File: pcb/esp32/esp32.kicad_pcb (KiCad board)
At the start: 2 copper layers, 15 parts, among them J1 Conn_01x02_Female, J2 Conn_01x15_Female, J3 Screw_Terminal_01x02, J4 Conn_01x15_Female, J5 Conn_01x15_Female, J6 Conn_01x02_Female, J6der1 Conn_01x15_Female, J7 Conn_01x02_Female, J7der1 Conn_01x15_Female, J8 Conn_01x02_Female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

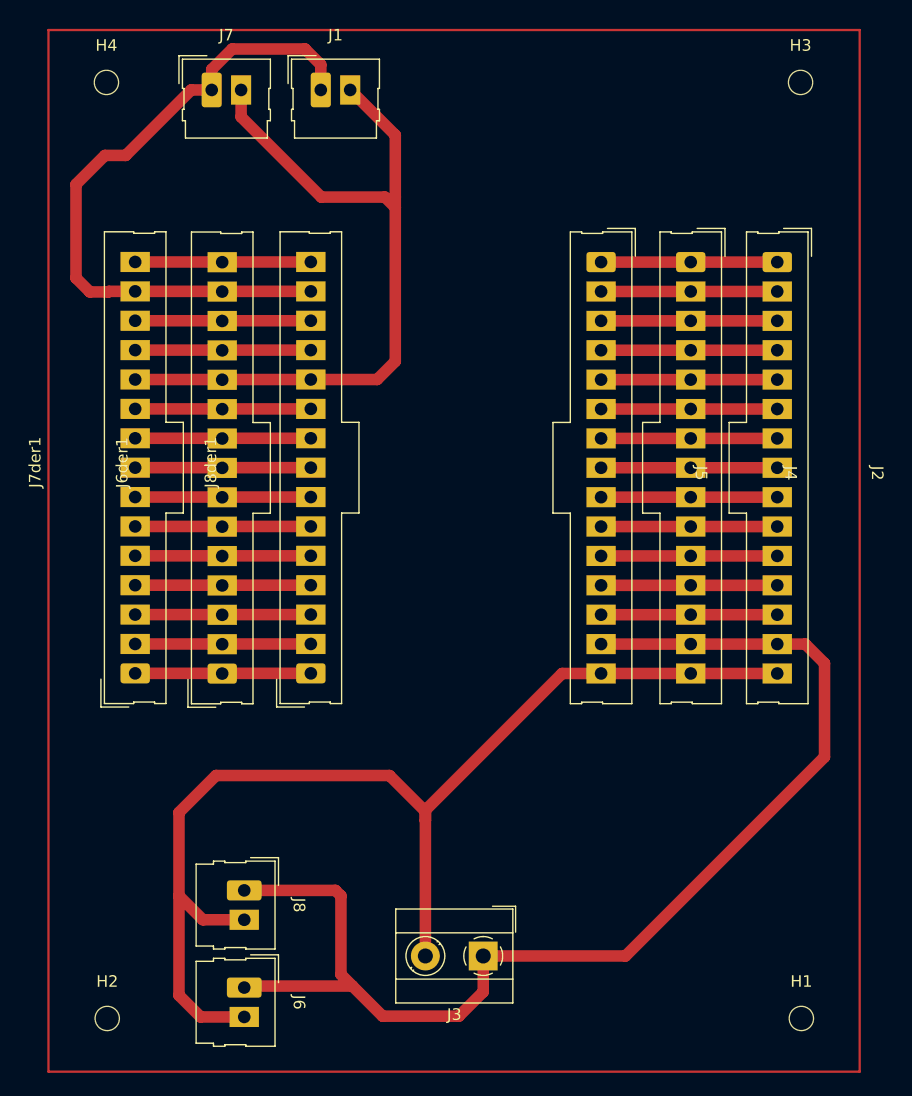
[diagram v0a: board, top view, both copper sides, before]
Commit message: added diode to esp32 board and updated solar board to fixed 5.0v ams1117
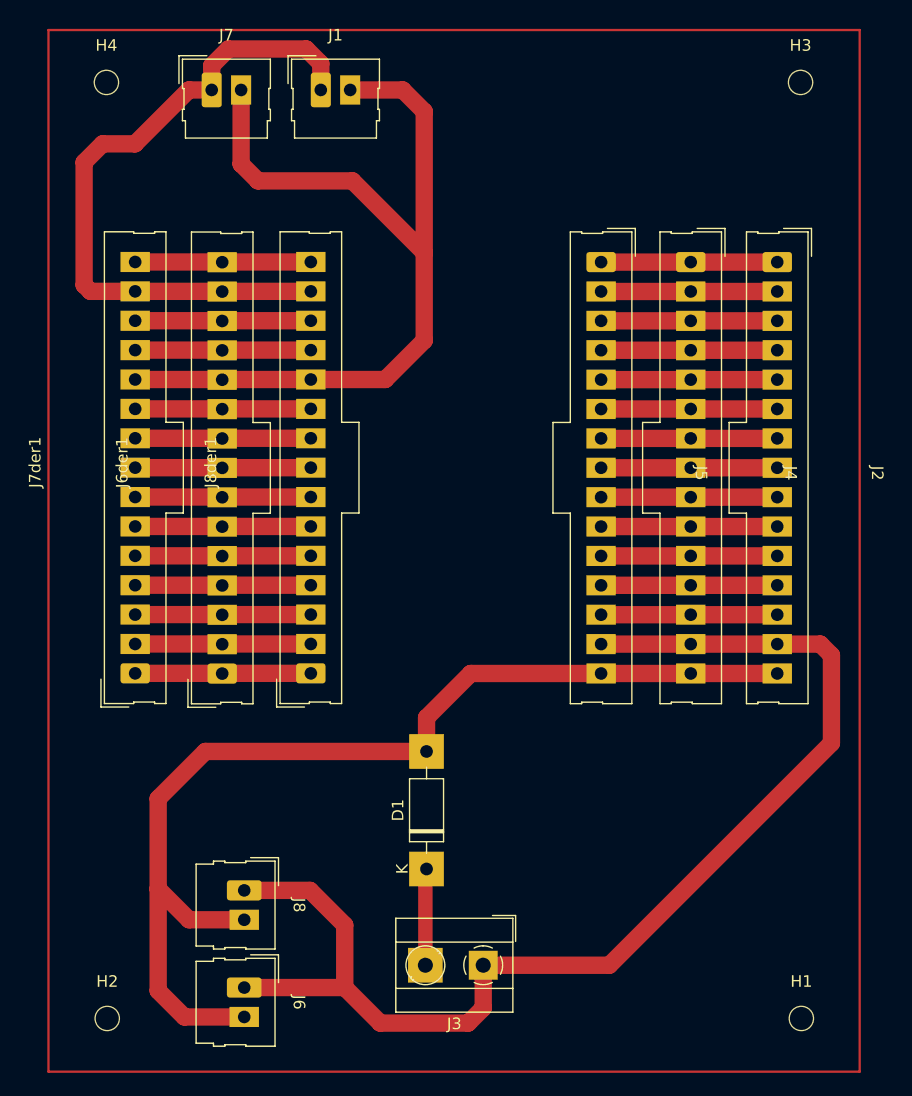
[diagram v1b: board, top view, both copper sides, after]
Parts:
- added D1: 1N4001, Diode_THT:D_DO-41_SOD81_P10.16mm_Horizontal, F.Cu at (137.6, 136.5)
- moved J3 0.80 mm to (142.5, 144.8)
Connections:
- J3 pad 2: VIN -> Net-(J3-Pad2)
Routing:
- net D21: track 67.1 -> 78.8 mm
- net Net-(J3-Pad2): track 0.00 -> 8.36 mm
- net VIN: track 101.3 -> 93.2 mm

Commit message: added new pins to connect more 3.3v sensors and 5.0v sensors, also added 2 pull up resistors for sda and scl pins
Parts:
- added J10: Conn_01x02_Female, esp32_ur:Connector_Molex_Molex_SL_171971-0004_1x02_P2.54mm_Vertical_squares, F.Cu at (149.3, 69.8)
- added J11: Conn_01x02_Female, esp32_ur:Connector_Molex_Molex_SL_171971-0004_1x02_P2.54mm_Vertical_squares, F.Cu at (156.9, 69.8)
- added J12: Conn_01x02_Female, esp32_ur:Connector_Molex_Molex_SL_171971-0004_1x02_P2.54mm_Vertical_squares, F.Cu at (126.2, 69.8)
- added J13: Conn_01x02_Female, esp32_ur:Connector_Molex_Molex_SL_171971-0004_1x02_P2.54mm_Vertical_squares, F.Cu at (121.9, 140.0)
- added J9: Conn_01x02_Female, esp32_ur:Connector_Molex_Molex_SL_171971-0004_1x02_P2.54mm_Vertical_squares, F.Cu at (141.7, 69.8)
- added R1: R, Resistor_THT:R_Axial_DIN0204_L3.6mm_D1.6mm_P5.08mm_Horizontal, F.Cu at (166.8, 71.4)
- added R2: R, Resistor_THT:R_Axial_DIN0204_L3.6mm_D1.6mm_P7.62mm_Horizontal, F.Cu at (116.4, 130.2)
- moved J8 19.4 mm to (106.7, 140.0), turned to 90 degrees
- moved J6 14.2 mm to (114.4, 140.0), turned to 90 degrees
- moved J1 12.1 mm to (118.7, 69.8), turned to 90 degrees
- moved J7 10.4 mm to (111.1, 69.8), turned to 90 degrees
- moved D1 4.60 mm to (142.2, 136.5)
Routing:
- net 3V3: track 15.2 -> 108.6 mm
- net GND2: track 15.2 -> 91.8 mm
- net D22: track 59.0 -> 101.3 mm
- net VIN: track 93.2 -> 68.8 mm
- net D21: track 78.8 -> 97.4 mm
- net Net-(D1-Pad1): track 8.36 -> 12.0 mm

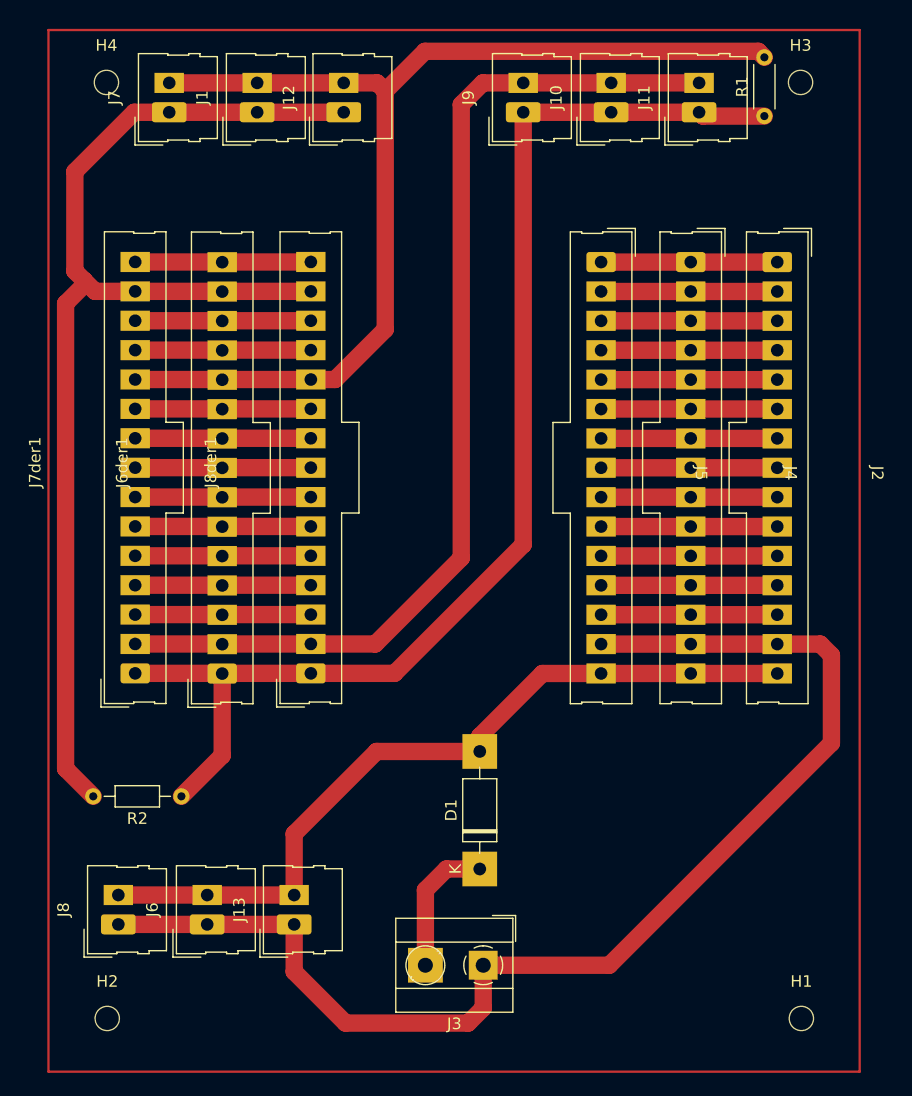
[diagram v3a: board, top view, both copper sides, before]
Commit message: changed the pull up from 5v to 3.3v
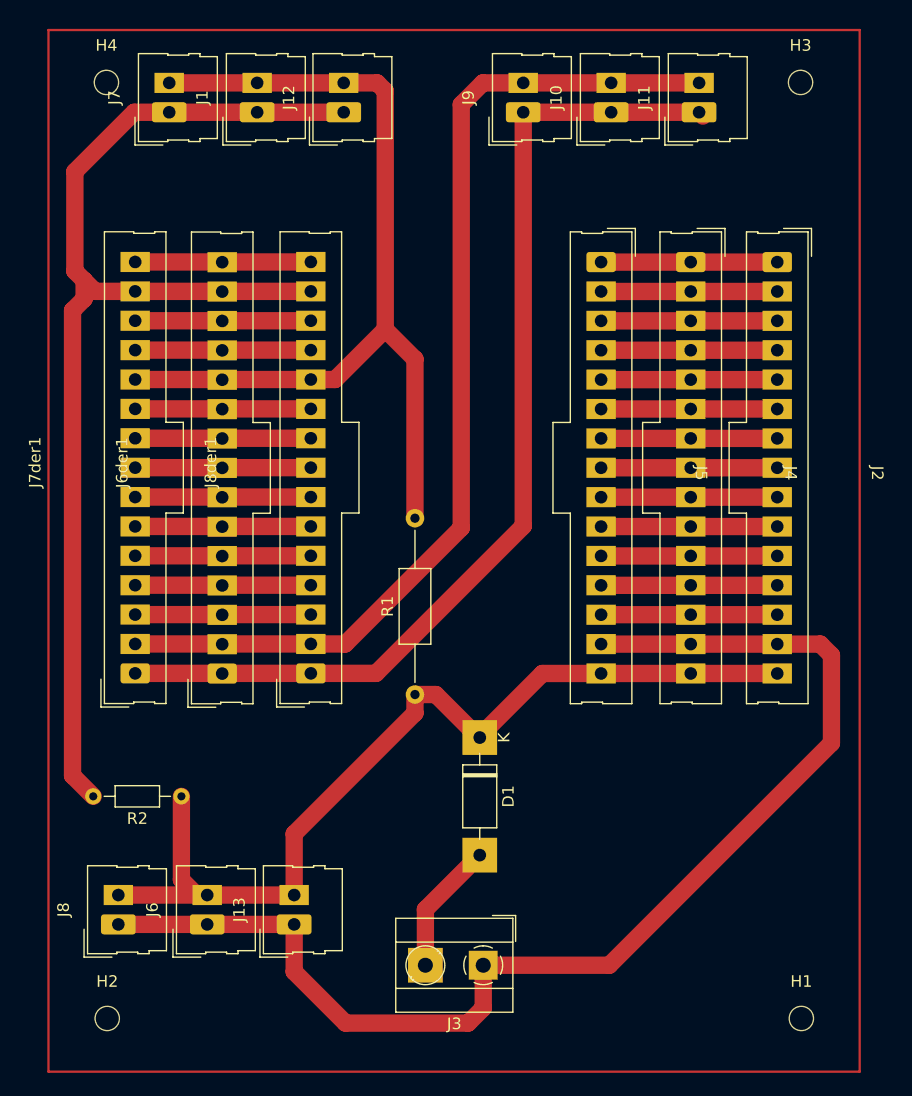
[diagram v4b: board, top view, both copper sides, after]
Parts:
- R1: footprint Resistor_THT:R_Axial_DIN0204_L3.6mm_D1.6mm_P5.08mm_Horizontal -> Resistor_THT:R_Axial_DIN0207_L6.3mm_D2.5mm_P15.24mm_Horizontal
- moved R1 58.4 mm to (136.6, 121.4)
- moved D1 11.4 mm to (142.2, 125.1), turned to -90 degrees
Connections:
- D1 pad 1: Net-(D1-Pad1) -> VIN
- D1 pad 2: VIN -> Net-(J3-Pad2)
- J3 pad 2: Net-(D1-Pad1) -> Net-(J3-Pad2)
- R1 pad 1: 3V3 -> VIN
- R2 pad 1: 3V3 -> VIN
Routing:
- net 3V3: track 108.6 -> 90.3 mm
- net D21: track 97.4 -> 80.4 mm
- net VIN: track 68.8 -> 81.2 mm
- net Net-(D1-Pad1): track 12.0 -> 0.00 mm
- net Net-(J3-Pad2): track 0.00 -> 11.5 mm
- net GND2: track 91.8 -> 90.3 mm
